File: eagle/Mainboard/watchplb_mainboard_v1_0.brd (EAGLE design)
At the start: 100 x 100 mm, 216 parts, among them IC1 LT1513, IC2 BM70BLES1FC2-0B03AA, IC3 LM1117DTX-ADJ-12V, IC4 AX5031, IC5 LM1117DTX-ADJ-10V, IC6 LM1117DTX-ADJ-3V3, J3 BNCPTH, Q1 8MHz / LFXTAL020423Reel, Q2 BC817-25SMD, Q3 DMN3023L-7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

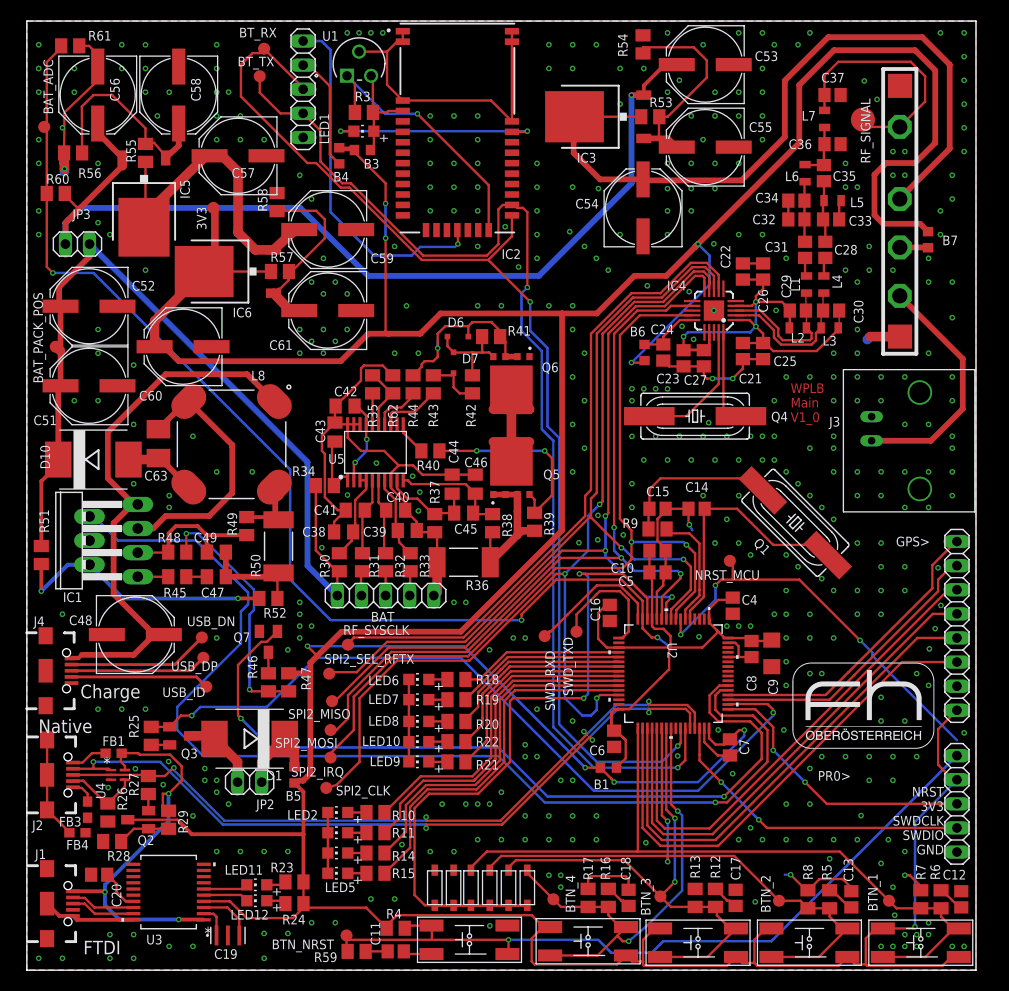
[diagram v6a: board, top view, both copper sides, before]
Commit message: einige kleine Änderungen: mcp111 ist smd massen verbinden taster footprint richtig orientierungspunkt U5 BQ ding richtungsmarkierung bei diode im Bat prot reset leitung bei pin verbinden LED rs auf 470R Charger SS pin mit pullup damits ohne firmware geht beschriftung am programmierheader verrutscht positiv beschriftung akkustecker usb 5v der unteren beiden trennen
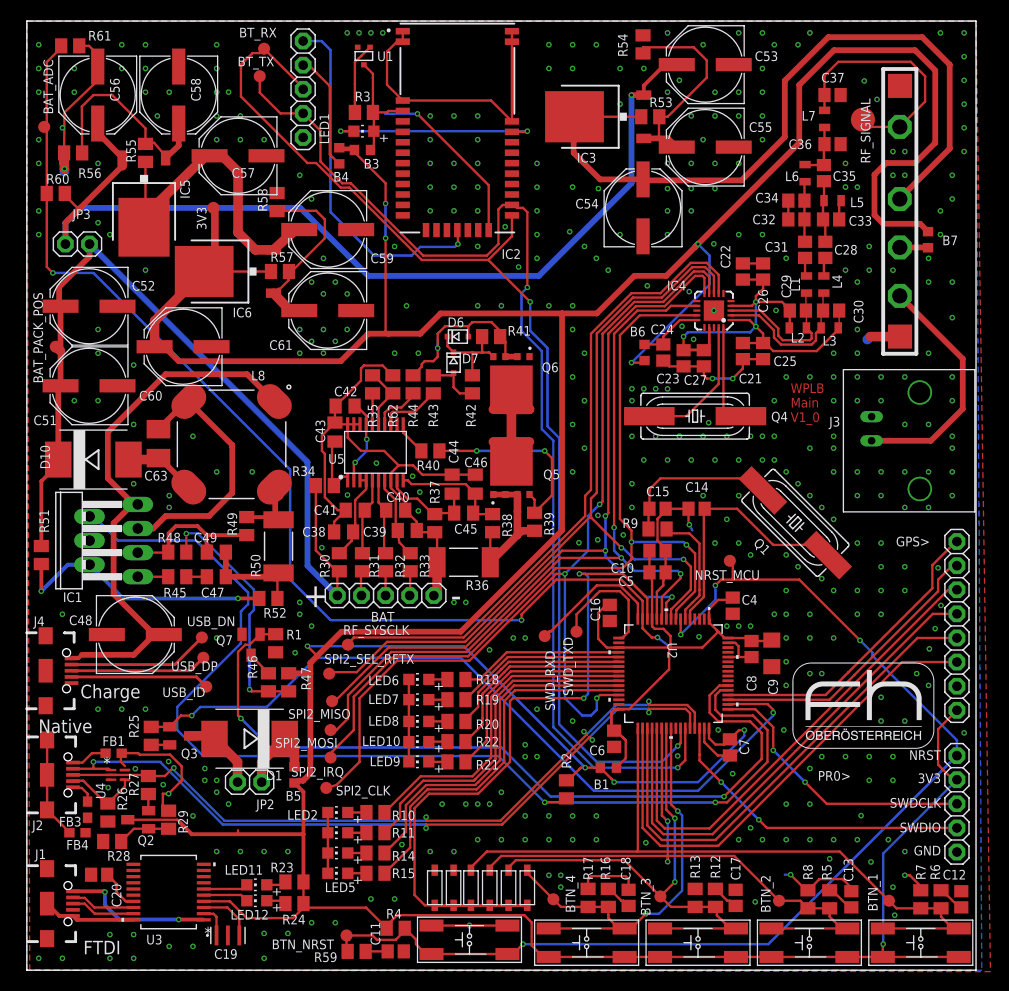
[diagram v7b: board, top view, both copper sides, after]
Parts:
- added R1, R2: 100k, resistor:M0805
- U1: value MCP111-XXXXX/TO -> MCP111-XXXXX/TOSMD; device MCP111-XXXTO:TO-92_MC -> MCP111-XXXTO:SC70-3-R
- moved Q7 1.85 mm to (23.6, 34.3)
- moved U1 0.89 mm to (35.5, 96.3), turned to 180 degrees
- moved S5 0.22 mm to (59.0, 2.90)
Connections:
- removed net +5V: FB1.2, J1.VBUS, R29.1, U3.1, U4.5
- new net N$41: J1.VBUS, U3.1
- new net N$44: FB1.2, R29.1, U4.5
- net +3V3: now also R2.2, S2.P$1, S2.P$2, S3.P$1, S3.P$2, S4.P$1, S4.P$2, S5.P$1, S5.P$2; no longer S2.P$3, S2.P$4, S3.P$3, S3.P$4, S4.P$3, S4.P$4, S5.P$3, S5.P$4
- net BTN_1: now also S2.P$3, S2.P$4; no longer S2.P$1, S2.P$2
- net BTN_2: now also S3.P$3, S3.P$4; no longer S3.P$1, S3.P$2
- net BTN_3: now also S4.P$3, S4.P$4; no longer S4.P$1, S4.P$2
- net BTN_4: now also S5.P$3, S5.P$4; no longer S5.P$1, S5.P$2
- net CHARGER_CH_PRECH: now also R1.1
- net CHARGER_SS: now also R2.1
- net GND: now also R1.2, S1.P$3, S1.P$4; no longer S1.P$1, S1.P$2
- net NRST: now also S1.P$1, S1.P$2; no longer S1.P$3, S1.P$4
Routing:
- net +5V: track 44.0 -> 0.00 mm, vias 3 -> 0
- net +3V3: track 497.7 -> 478.5 mm
- net N$41: track 0.00 -> 15.8 mm, vias 0 -> 2
- net N$44: track 0.00 -> 14.6 mm, vias 0 -> 1
- net GND: track 183.5 -> 186.3 mm, vias 417 -> 402
- net BTN_4: track 49.6 -> 47.0 mm
- net CHARGER_SS: track 117.5 -> 120.0 mm, vias 1 -> 2
- net BT_NRST: track 28.6 -> 26.3 mm
- net INT_POWER: track 51.9 -> 53.9 mm
- net NRST: track 124.8 -> 122.9 mm
- net N$80: track 11.3 -> 12.8 mm
- net BTN_2: track 66.3 -> 65.1 mm
- net BTN_1: track 78.5 -> 77.3 mm
- net BTN_3: track 56.0 -> 54.7 mm
- net SPI2_MISO: track 84.3 -> 85.1 mm
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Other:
- board text added: "+"
- board text added: "-"
- board text added: "3V3"
- board text added: "GND"
- board text added: "NRST"
- board text added: "SWDCLK"
- board text added: "SWDIO"
- board text removed: "NRST 3V3 SWDCLK SWDIO GND"

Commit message: + started doku
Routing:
- net BAT_ADC: track 118.7 -> 114.2 mm, vias 3 -> 2
- net V+STM: track 61.1 -> 62.7 mm
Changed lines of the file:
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@@
 <attribute name="VENDOR" value="STMicroelectronics" x="68.1228" y="31.242" size="1.778" layer="27" rot="R270" display="off"/>
 <attribute name="MANUFACTURER_PART_NUMBER" value="stm32l0x3rl" x="68.1228" y="31.242" size="1.778" layer="27" rot="R270" display="off"/>
-<attribute name="NAME" x="67.4878" y="34.5186" size="1.016" layer="25" font="vector" rot="SR270"/>
+<attribute name="NAME" x="65.3034" y="32.2834" size="1.016" layer="25" font="vector" rot="SR0"/>
 </element>
 <element name="C4" library="resistor" package="C0805" value="100nF" x="74.3712" y="38.4048" smashed="yes" rot="R270">
@@
 <wire x1="65.8728" y1="36.2352" x2="66.1416" y2="35.9664" width="0.254" layer="1"/>
 <wire x1="66.1416" y1="35.9664" x2="67.056" y2="35.9664" width="0.254" layer="1"/>
-<wire x1="67.056" y1="35.9664" x2="67.818" y2="35.2044" width="0.254" layer="1"/>
-<wire x1="67.818" y1="35.2044" x2="67.818" y2="33.992" width="0.254" layer="1"/>
 <wire x1="66.7512" y1="30.7848" x2="67.6656" y2="31.6992" width="0.254" layer="1"/>
-<wire x1="67.6656" y1="31.6992" x2="67.6656" y2="33.992" width="0.254" layer="1"/>
+<wire x1="67.6656" y1="31.6992" x2="67.6656" y2="33.6804" width="0.254" layer="1"/>
+<wire x1="67.6656" y1="33.6804" x2="67.6656" y2="33.992" width="0.254" layer="1"/>
+<wire x1="67.056" y1="35.9664" x2="67.6656" y2="35.3568" width="0.254" layer="1"/>
+<wire x1="67.6656" y1="35.3568" x2="67.6656" y2="34.29" width="0.254" layer="1"/>
+<wire x1="67.6656" y1="34.29" x2="67.6656" y2="33.992" width="0.254" layer="1"/>
+<wire x1="67.3608" y1="33.9852" x2="67.6656" y2="34.29" width="0.254" layer="1"/>
+<wire x1="67.6656" y1="34.29" x2="67.9704" y2="33.9852" width="0.254" layer="1"/>
+<wire x1="67.9704" y1="33.9852" x2="67.6656" y2="33.6804" width="0.254" layer="1"/>
+<wire x1="67.6656" y1="33.6804" x2="67.3608" y2="33.9852" width="0.254" layer="1"/>
 </signal>
 <signal name="N$78">
@@
 <wire x1="1.8288" y1="88.8492" x2="1.9456" y2="88.8492" width="0.254" layer="1"/>
 <wire x1="1.9456" y1="88.8492" x2="2.098" y2="89.0016" width="0.254" layer="1"/>
-<wire x1="64.8728" y1="36.992" x2="64.8728" y2="36.016" width="0.254" layer="1"/>
-<wire x1="64.8728" y1="36.016" x2="65.8368" y2="35.052" width="0.254" layer="1"/>
-<wire x1="65.8368" y1="35.052" x2="66.4464" y2="35.052" width="0.254" layer="1"/>
-<via x="66.4464" y="35.052" extent="1-16" drill="0.3048" shape="octagon"/>
-<wire x1="66.4464" y1="35.052" x2="67.6656" y2="34.1376" width="0.254" layer="16"/>
 <wire x1="2.098" y1="81.8388" x2="2.098" y2="74.102" width="0.254" layer="1"/>
 <wire x1="2.098" y1="74.102" x2="2.7432" y2="73.4568" width="0.254" layer="1"/>
